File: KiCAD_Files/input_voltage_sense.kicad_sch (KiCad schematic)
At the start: 5 parts, among them U701 MCP6486UT-E/LT

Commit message: First routing pass complete.
Signed-off-by: Jean Alinei <jean.alinei@owntech.org>
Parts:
- C701: footprint (none) -> Capacitor_SMD:C_0805_2012Metric
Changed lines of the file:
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@@
 			)
 		)
-		(property "Footprint" ""
+		(property "Footprint" "Capacitor_SMD:C_0805_2012Metric"
 			(at 75.8952 105.41 0)
 			(effects

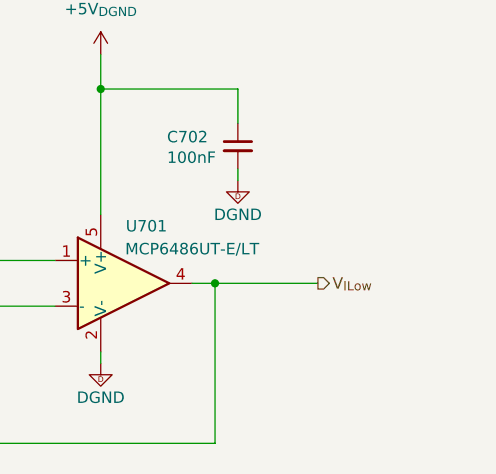
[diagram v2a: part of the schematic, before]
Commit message: Added DRC rules according to IEC60664 and IPC2221.
Signed-off-by: Jean Alinei <jean.alinei@owntech.org>
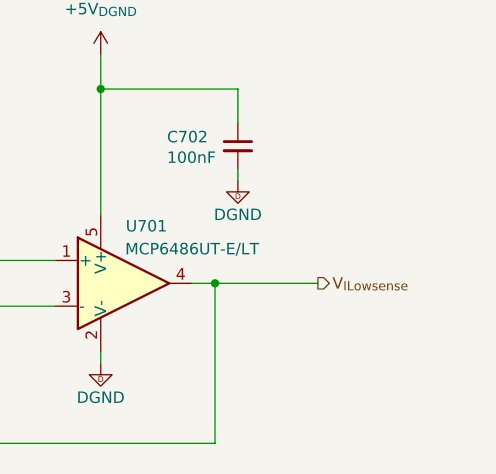
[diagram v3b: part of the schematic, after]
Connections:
- net V_{ILow} renamed V_{ILowsense}
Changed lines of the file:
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@@
 		)
 	)
-	(hierarchical_label "V_{ILow}"
+	(hierarchical_label "V_{ILowsense}"
 		(shape output)
 		(at 121.92 93.98 0)

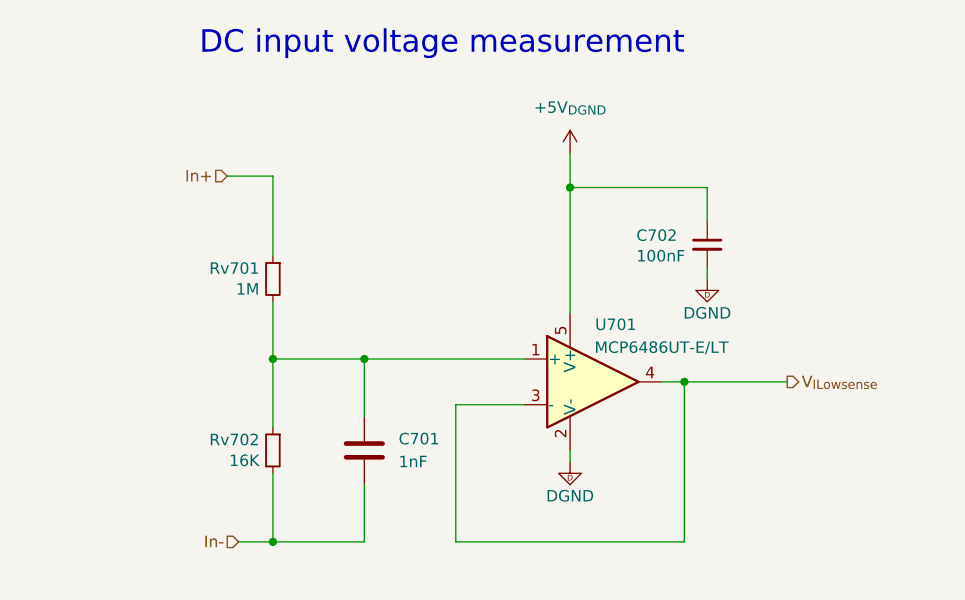
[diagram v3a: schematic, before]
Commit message: Added passive references. Added ESD protection for MCU pins.
Signed-off-by: Jean Alinei <jean.alinei@owntech.org>
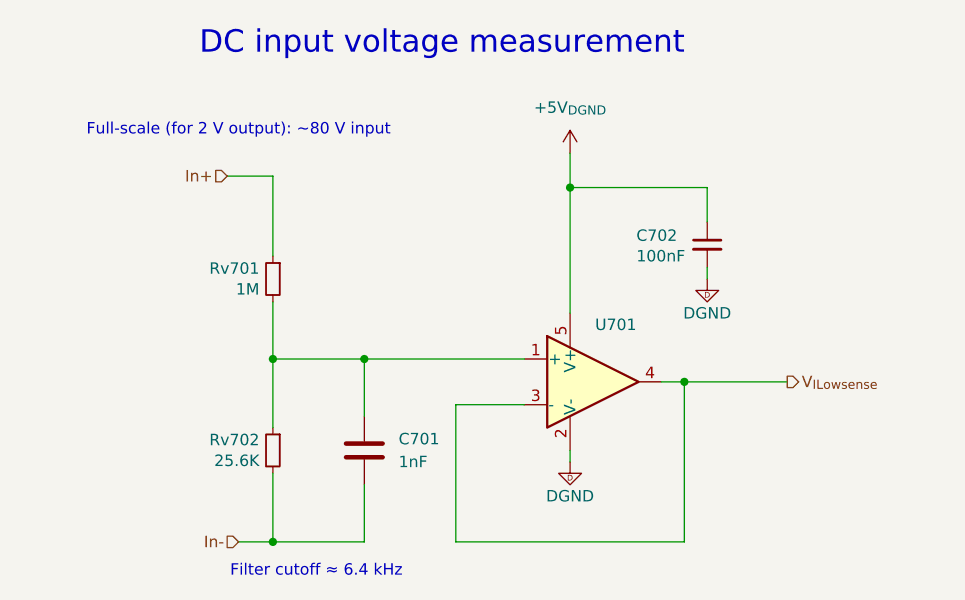
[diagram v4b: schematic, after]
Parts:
- C701: LCSC (none) -> C46653
- C702: Dielectric X7R -> (none); LCSC C5449000 -> C49678; Package 1206 -> (none); Voltage 50V -> (none); manf# C1206C104K5RAC7867 -> (none)
- Rv701: LCSC (none) -> C17514
- Rv702: value 16K -> 25.6K; LCSC (none) -> C46670
- U701: Rotation Offset (none) -> 90; Subfunction IILow Measure -> (none); manf# MCP6486UT-E/LT -> (none)
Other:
- note added: "Filter cutoff ≈ 6.4 kHz"
- note added: "Full-scale (for 2 V output): ~80 V input"
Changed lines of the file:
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@@
 	(generator_version "9.0")
 	(paper "A3")
+	(text "Filter cutoff ≈ 6.4 kHz"
+		(exclude_from_sim no)
+		(at 69.596 115.062 0)
+		(effects
+			(font
+				(size 1.27 1.27)
+			)
+		)
+	)
 	(text "DC input voltage measurement"
 		(exclude_from_sim no)
@@
 			(font
 				(size 2.5 2.5)
+			)
+		)
+	)
+	(text "Full-scale (for 2 V output): ~80 V input"
+		(exclude_from_sim no)
+		(at 60.96 66.04 0)
+		(effects
+			(font
+				(size 1.27 1.27)
 			)
 		)
@@
 			)
 		)
-		(property "Value" "16K"
+		(property "Value" "25.6K"
 			(at 63.2714 102.743 0)
 			(effects
@@
 			)
 		)
-		(property "LCSC" ""
+		(property "LCSC" "C46670"
 			(at 64.77 101.6 0)
 			(effects
@@
 			)
 		)
-		(property "LCSC" ""
+		(property "LCSC" "C17514"
 			(at 64.77 82.55 0)
 			(effects
@@
 			)
 		)
-		(property "DNP" ""
-			(at 97.79 93.98 0)
-			(effects
-				(font
-					(size 1.27 1.27)
-				)
-				(hide yes)
-			)
-		)
-		(property "manf#" "MCP6486UT-E/LT"
-			(at 107.95 90.17 0)
-			(effects
-				(font
-					(size 1.27 1.27)
-				)
-			)
-		)
 		(property "Functional Block" "Measurement"
 			(at 90.17 86.36 0)
@@
 			)
 		)
-		(property "Metal content" ""
+		(property "LCSC" "C5224800"
 			(at 97.79 93.98 0)
 			(effects
@@
 			)
 		)
-		(property "Subfunction" "IILow Measure"
-			(at 107.95 97.79 0)
-			(effects
-				(font
-					(size 1.27 1.27)
-				)
-				(hide yes)
-			)
-		)
-		(property "Technology" ""
-			(at 97.79 93.98 0)
-			(effects
-				(font
-					(size 1.27 1.27)
-				)
-				(hide yes)
-			)
-		)
-		(property "LCSC" "C5224800"
+		(property "Rotation Offset" "90"
 			(at 97.79 93.98 0)
 			(effects
@@
 			)
 		)
+		(property "LCSC" "C46653"
+			(at 74.93 101.6 0)
+			(effects
+				(font
+					(size 1.27 1.27)
+				)
+				(hide yes)
+			)
+		)
 		(pin "1"
 		)
@@
 			)
 		)
-		(property "manf#" "C1206C104K5RAC7867"
+		(property "LCSC" "C49678"
 			(at 113.03 78.74 0)
 			(effects
-				(font
-					(size 1.27 1.27)
-				)
-				(hide yes)
-			)
-		)
-		(property "DNP" ""
-			(at 113.03 78.74 0)
-			(effects
-				(font
-					(size 1.27 1.27)
-				)
-				(hide yes)
-			)
-		)
-		(property "Voltage" "50V"
-			(at 111.76 82.55 90)
-			(effects
-				(font
-					(size 1.27 1.27)
-				)
-				(hide yes)
-			)
-		)
-		(property "Package" "1206"
-			(at 115.57 82.55 90)
-			(effects
-				(font
-					(size 1.27 1.27)
-				)
-				(hide yes)
-			)
-		)
-		(property "Dielectric" "X7R"
-			(at 113.03 78.74 0)
-			(effects
-				(font
-					(size 1.27 1.27)
-				)
-				(hide yes)
-			)
-		)
-		(property "Technology" ""
-			(at 113.03 78.74 0)
-			(effects
-				(font
-					(size 1.27 1.27)
-				)
-				(hide yes)
-			)
-		)
-		(property "LCSC" "C5449000"
-			(at 113.03 78.74 0)
-			(effects

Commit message: Added TL431 for AC measurement 5V regulation. Added more film capacitance. Increased size of 100V ceramic caps to 1210.
Signed-off-by: Jean Alinei <jean.alinei@owntech.org>
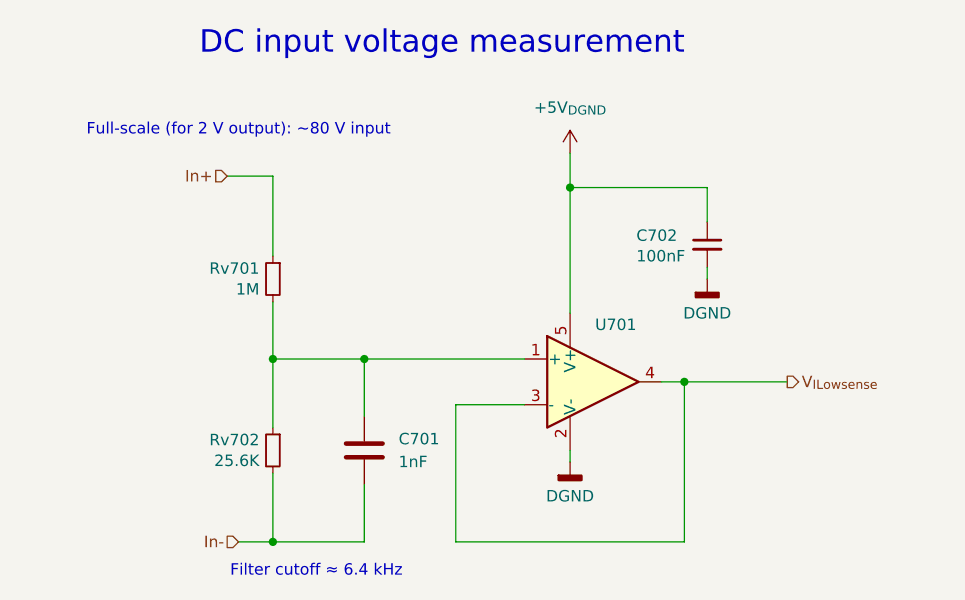
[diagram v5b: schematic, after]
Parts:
- U701: footprint Package_TO_SOT_SMD:SOT-353_SC-70-5_Handsoldering -> Package_TO_SOT_SMD:SOT-353_SC-70-5; symbol Symbols:MCP6486UT-E/LT -> Symbols:MCP6486UT-E/LT
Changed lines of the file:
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@@
 	)
 	(symbol
-		(lib_id "Symbols:DGND")
+		(lib_id "power:GNDD")
 		(at 113.03 82.55 0)
 		(unit 1)
@@
 			)
 		)
-		(property "Description" ""
+		(property "Description" "Power symbol creates a global label with name \"GNDD\" , digital ground"
 			(at 113.03 82.55 0)
 			(effects
@@
 	)
 	(symbol
-		(lib_id "Symbols:DGND")
+		(lib_id "power:GNDD")
 		(at 97.79 102.87 0)
 		(unit 1)
@@
 			)
 		)
-		(property "Description" ""
+		(property "Description" "Power symbol creates a global label with name \"GNDD\" , digital ground"
 			(at 97.79 102.87 0)
 			(effects
@@
 	)
 	(symbol
-		(lib_id "Symbols:+12V_PGND")
+		(lib_id "power:+12V")
 		(at 97.79 68.58 0)
 		(unit 1)
 		(exclude_from_sim no)
-		(in_bom no)
-		(on_board no)
+		(in_bom yes)
+		(on_board yes)
 		(dnp no)
 		(fields_autoplaced yes)
@@
 		)
 		(property "Footprint" ""
-			(at 100.965 66.04 0)
+			(at 97.79 68.58 0)
 			(effects
 				(font
@@
 		)
 		(property "Datasheet" ""
-			(at 100.965 66.04 0)
-			(effects
-				(font
-					(size 1.27 1.27)
-				)
-				(hide yes)
-			)
-		)
-		(property "Description" ""
+			(at 97.79 68.58 0)
+			(effects
+				(font
+					(size 1.27 1.27)
+				)
+				(hide yes)
+			)
+		)
+		(property "Description" "Power symbol creates a global label with name \"+12V\""
 			(at 97.79 68.58 0)
 			(effects
@@
 			)
 		)
-		(property "Description" ""
+		(property "Description" "Resistor, small symbol"
 			(at 64.77 101.6 0)
 			(effects
@@
 			)
 		)
-		(property "Description" ""
+		(property "Description" "Resistor, small symbol"
 			(at 64.77 82.55 0)
 			(effects
@@
 	)
 	(symbol
-		(lib_id "Symbols:MCP6486UT-E/LT ")
+		(lib_id "Symbols:MCP6486UT-E/LT")
 		(at 97.79 93.98 0)
 		(unit 1)
@@
 			)
 		)
-		(property "Footprint" "Package_TO_SOT_SMD:SOT-353_SC-70-5_Handsoldering"
+		(property "Footprint" "Package_TO_SOT_SMD:SOT-353_SC-70-5"
 			(at 102.87 100.33 0)
 			(effects

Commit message: Tidied up the schematic. Added the pdf version for V0.9.
Signed-off-by: Jean Alinei <jean.alinei@owntech.org>
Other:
- title: (none) -> DC Input voltage measurement
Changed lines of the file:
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@@
 	(generator "eeschema")
 	(generator_version "9.0")
-	(paper "A3")
+	(paper "A4")
+	(title_block
+		(title "DC Input voltage measurement")
+		(date "2026-01-27")
+		(comment 1 "JAL")
+		(comment 2 "JAL")
+		(comment 3 "JAL")
+	)
 	(text "Filter cutoff ≈ 6.4 kHz"
 		(exclude_from_sim no)
